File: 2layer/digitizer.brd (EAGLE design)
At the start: 88.9 x 88.9 mm, 40 parts, among them X1 SMA-142-0711-881/886

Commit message: started layout2
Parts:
- removed JP2: (no value), pinhead:1X10
- added X2: SMA-142-0711-881/886, con-coax:J502-ND-142-0711-881/886
- JP1: device pinhead:1X10 -> pinhead:2X20
- moved U$5 93.7 mm to (46.2, 44.0)
- moved JP1 69.7 mm to (-6.35, -88.6)
- moved C8 6.10 mm to (56.6, 35.3), turned to 270 degrees
- moved C7 4.75 mm to (58.2, 35.3), turned to 270 degrees
- moved C5 3.64 mm to (57.4, 37.3), turned to 0 degrees
- moved C6 3.45 mm to (57.4, 38.6), turned to 0 degrees
- moved X1 0.25 mm to (52.6, 88.4)
- moved C2 0.25 mm to (59.9, 37.6)
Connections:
- removed net SDC_OEN: JP2.4
- net ADC_SLP: no longer JP2.3
- net OVFL: no longer JP2.2
- net SAMP0: no longer JP1.1
- net SAMP1: no longer JP1.2
- net SAMP2: no longer JP1.3
- net SAMP3: no longer JP1.4
- net SAMP4: no longer JP1.5
- net SAMP5: no longer JP1.6
- net SAMP6: no longer JP1.7
- net SAMP7: no longer JP1.8
- net SAMP8: no longer JP1.9
- net SAMP9: no longer JP1.10
- net SAMPCLK: no longer JP2.1
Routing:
- net GND: track 5.53 -> 0.00 mm, vias 0 -> 8
- net AVDD: track 1.92 -> 0.00 mm

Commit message: starting final layout
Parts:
- added C15: (no value), rcl:C0402
- added C16, C17: 18p, resistor:C0402
- added C18, C19, C21: 0.1u, resistor:C0402
- added C20: 1u, resistor:C0402
- added C22: 4.7u, resistor:C0402
- added IC1: FT601QQFN76, lt_ftdi_and_more:QFN76
- added JP2: (no value), pinhead:2X20
- added JP3: (no value), pinhead:1X04
- added R10, R12, R13, R16, R17: (no value), resistor:R0402
- added R11: (no value), resistor:V234/12
- added R14, R15: 0, resistor:R0805
- added S1, S2: MOMENTARY-SWITCH-SPST-SMD-6.0X3.5MM, SparkFun-Switches:TACTILE_SWITCH_SMD_6.0X3.5MM
- added U$6: USB3.0, components:USB-MICROB-3.0
- added U$7: CX3225SB_UKY1C-H1-16357-0045, components:UKY1C-H1-16357-0045
- Z10, Z3, Z4, Z5: device components:R0805 -> components:R0402
- moved X2 147.9 mm to (0.51, 20.3)
- moved JP1 126.7 mm to (48.3, 25.7), turned to 90 degrees
- moved R6 97.8 mm to (17.5, 8.89), turned to 90 degrees
- moved X1 97.2 mm to (0.51, 6.35), turned to 0 degrees
- moved R7 96.7 mm to (17.5, 2.79), turned to 90 degrees
- moved Z11 91.3 mm to (17.5, 5.84), turned to 270 degrees
- moved R5 91.1 mm to (7.11, 2.29)
- moved Z6 88.2 mm to (7.11, 6.60), turned to 90 degrees
- moved Z10 85.8 mm to (18.8, 3.81), turned to 90 degrees
- moved Z8 84.1 mm to (9.37, 2.27), turned to 270 degrees
- moved C14 83.9 mm to (21.6, 9.91), turned to 270 degrees
- moved Z5 83.5 mm to (18.8, 6.86), turned to 270 degrees
- moved Z7 82.8 mm to (9.40, 6.60), turned to 90 degrees
- moved C13 82.4 mm to (24.1, 9.91), turned to 270 degrees
- moved Z9 76.7 mm to (8.38, 10.4), turned to 0 degrees
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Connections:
- removed net N$27: R6.1
- removed net N$28: R7.1
- new net BE0: IC1.4
- new net BE1: IC1.5
- new net BE2: IC1.6
- new net BE3: IC1.7
- new net D+: IC1.23, U$6.P$3
- new net D-: IC1.25, U$6.P$2
- new net FCLK: IC1.58
- new net GPIO0: IC1.17
- new net GPIO1: IC1.18
- new net N$11: C16.2, IC1.21, U$7.P$1
- new net N$12: C17.2, IC1.22, U$7.P$3
- new net N$13: IC1.27, R10.2, R11.2
- new net N$14: C18.2, U$6.P$10
- new net N$15: C19.2, U$6.P$9
- new net N$16: R14.1, X2.1
- new net OEN: IC1.13
- new net OTG_ID: U$6.P$4
- new net RDN: IC1.12
- new net RFIN2: JP3.2, R7.1
- new net RSTN: IC1.15, R12.2, R17.1, S2.2
- new net RXFN: IC1.9
- new net SFT_RSTN: R17.2
- new net SFT_WKPN: R16.2
- new net SIWUN: IC1.10
- new net SSRX+: IC1.35, U$6.P$7
- new net SSRX-: IC1.34, U$6.P$6
- new net SSTX+: C18.1, IC1.32
- new net SSTX-: C19.1, IC1.31
- new net TXEN: IC1.8
- new net UDAT0: IC1.40
- new net UDAT1: IC1.41
- new net UDAT10: IC1.52
- new net UDAT11: IC1.53
- new net UDAT12: IC1.54
- new net UDAT13: IC1.55
- new net UDAT14: IC1.56
- new net UDAT15: IC1.57
- new net UDAT16: IC1.60
- new net UDAT17: IC1.61
- new net UDAT18: IC1.62
- new net UDAT19: IC1.63
- new net UDAT2: IC1.42
- new net UDAT20: IC1.64
- new net UDAT21: IC1.65
- new net UDAT22: IC1.66
- new net UDAT23: IC1.67
- new net UDAT24: IC1.69
- new net UDAT25: IC1.70
- new net UDAT26: IC1.71
- new net UDAT27: IC1.72
- new net UDAT28: IC1.73
- new net UDAT29: IC1.74
- new net UDAT3: IC1.43
- new net UDAT30: IC1.75
- new net UDAT31: IC1.76
- new net UDAT4: IC1.44
- new net UDAT5: IC1.45
- new net UDAT6: IC1.46
- new net UDAT7: IC1.47
- new net UDAT8: IC1.50
- new net UDAT9: IC1.51
- new net V1REF: C15.2, C22.1, IC1.2, IC1.3, IC1.30, IC1.33, IC1.39, IC1.48
- new net VBUS: IC1.37, U$6.P$1
- new net WKPN: IC1.16, R13.2, R16.1, S1.2
- new net WRN: IC1.11
- net AVDD: now also JP3.4, R12.1, R13.1
- net DVDD: now also C20.1, C21.1, IC1.14, IC1.20, IC1.24, IC1.28, IC1.38, IC1.49, IC1.59, IC1.68
- net GND: now also C15.1, C16.1, C17.1, C20.2, C21.2, C22.2, IC1.1, IC1.26, IC1.29, IC1.36, IC1.77, JP3.1, R10.1, R11.1, R15.1, S1.1, S2.1, U$6.P$11, U$6.P$12, U$6.P$5, U$6.P$8, U$7.P$2, U$7.P$4, X2.G@1, X2.G@2, X2.G@3, X2.G@4
- net LO+: now also R14.2
- net LO-: now also R15.2
- net MIX+: now also U$5.6
- net MIX-: now also U$5.5
- net RFIN: now also JP3.3, R6.1
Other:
- board size 88.9 x 88.9 mm -> 88.1 x 52.3 mm

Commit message: okawndpam
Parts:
- removed JP3: (no value), pinhead:1X04
- removed R14, R15: 0, resistor:R0805
- removed R5: 25, resistor:R0805
- removed Z6: 12p, resistor:C0805
- removed Z7, Z9: 0, components:R0805
- removed Z8: 0, resistor:C0805
- moved C16 74.5 mm to (15.2, 39.9), turned to 270 degrees
- moved U$7 70.7 mm to (18.3, 39.9), turned to 0 degrees
- moved C18 67.6 mm to (16.3, 43.9), turned to 90 degrees
- moved R10 67.3 mm to (11.4, 43.7), turned to 270 degrees
- moved R11 67.3 mm to (11.4, 43.7), turned to 270 degrees
- moved JP2 67.1 mm to (121.5, 26.7)
- moved C17 66.9 mm to (21.3, 39.9), turned to 90 degrees
- moved JP1 64.3 mm to (112.5, 26.9)
- moved C19 63.8 mm to (17.8, 43.9), turned to 90 degrees
- moved U$6 61.3 mm to (24.2, 47.1), turned to 180 degrees
- moved S2 59.0 mm to (2.79, 46.5), turned to 270 degrees
- moved R17 57.0 mm to (3.81, 40.1), turned to 270 degrees
- moved S1 56.9 mm to (7.11, 46.5), turned to 270 degrees
- moved R16 56.5 mm to (5.84, 39.9), turned to 270 degrees
- moved X1 55.5 mm to (55.6, 0.25), turned to 90 degrees
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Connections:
- removed net N$16: R14.1, X2.1
- removed net RFILT: Z7.2, Z8.1, Z9.1
- removed net RFIN: JP3.3, R6.1, Z9.2
- removed net RFIN2: JP3.2, R7.1
- net AVDD: no longer JP3.4
- net GND: now also JP1.11, JP1.12, JP1.21, JP1.22, JP1.31, JP2.21, JP2.22, JP2.31, JP2.32; no longer JP3.1, R15.1, X1.G@1, X1.G@2, X1.G@3, X1.G@4, X2.G@1, X2.G@2, X2.G@3, X2.G@4, Z6.2, Z8.2
- net LO+: now also X2.1; no longer R14.2
- net LO-: now also X2.G@1, X2.G@2, X2.G@3, X2.G@4; no longer R15.2
- net N$1: now also R7.1, X1.G@1, X1.G@2, X1.G@3, X1.G@4; no longer R5.2, Z6.1, Z7.1
- net N$10: now also R6.1; no longer R5.1
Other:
- board size 88.1 x 52.3 mm -> 75.7 x 51.3 mm

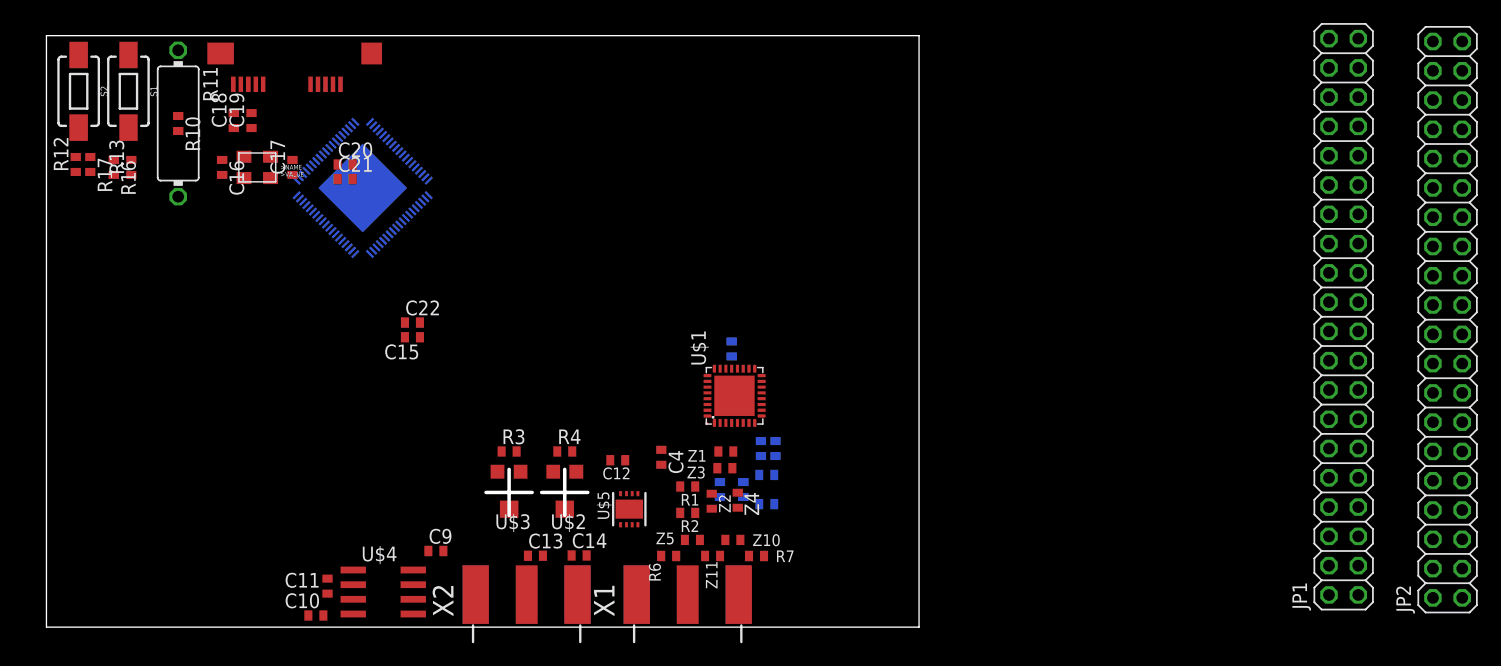
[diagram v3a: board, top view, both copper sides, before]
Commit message: moved guts to center to make more of a sheild-like adaptor to mate with MACH
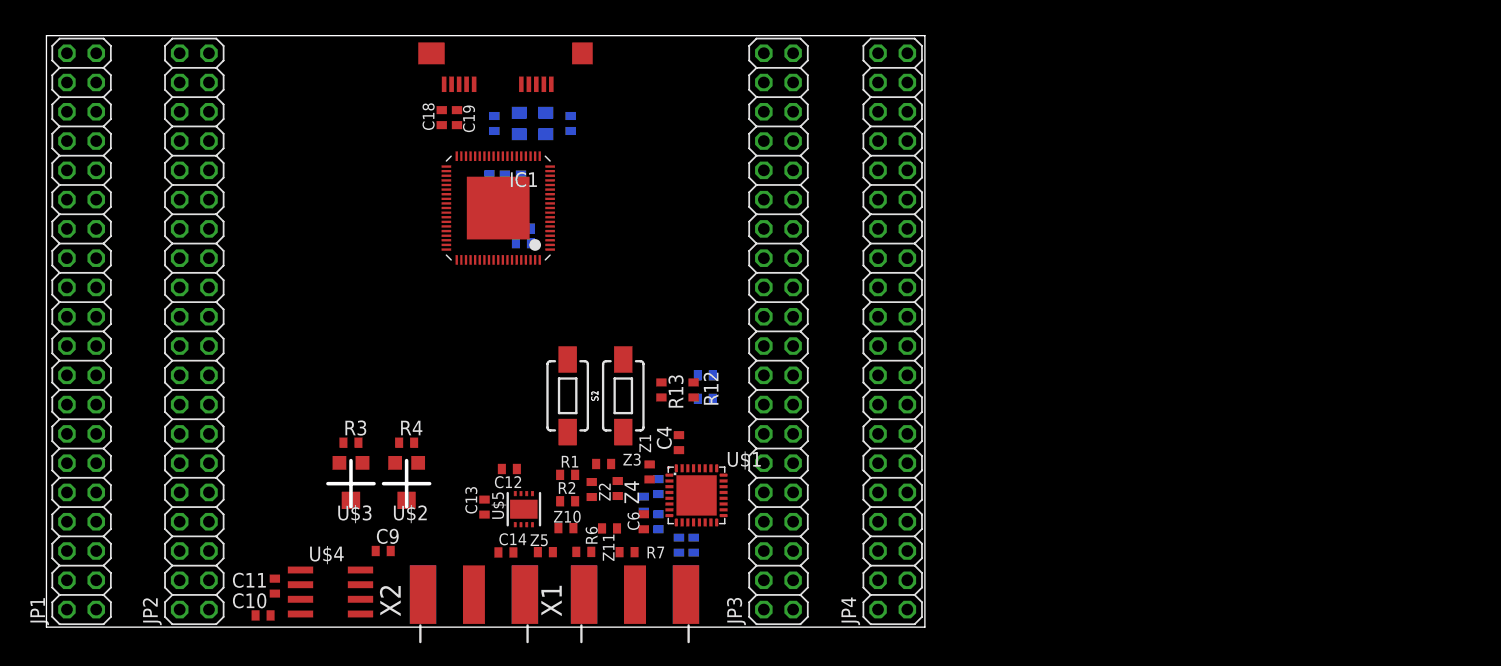
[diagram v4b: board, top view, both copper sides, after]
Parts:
- removed R11: (no value), resistor:V234/12
- added JP3, JP4: (no value), pinhead:2X20
- R10: value (none) -> 10k <=0.1%
- moved JP1 109.5 mm to (3.05, 25.7)
- moved JP2 108.7 mm to (12.8, 25.7)
- moved R17 57.1 mm to (57.1, 19.8), flipped to the bottom, turned to 180 degrees
- moved R12 57.1 mm to (56.1, 20.6), turned to 270 degrees
- moved R16 54.4 mm to (57.1, 21.8), flipped to the bottom, turned to 180 degrees
- moved S1 50.4 mm to (50.0, 20.1), turned to 90 degrees
- moved S2 50.0 mm to (45.2, 20.1), turned to 90 degrees
- moved R13 49.9 mm to (53.3, 20.6)
- moved C16 30.5 mm to (45.5, 43.7), flipped to the bottom
- moved R10 30.2 mm to (41.2, 38.6), flipped to the bottom, turned to 90 degrees
- moved U$7 24.2 mm to (42.2, 43.7), flipped to the bottom
- moved U$6 18.3 mm to (42.5, 47.1)
- moved C18 18.0 mm to (34.3, 44.2)
- moved C17 17.9 mm to (38.9, 43.7), flipped to the bottom
- moved C19 17.8 mm to (35.6, 44.2)
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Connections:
- net GND: no longer R11.1
- net N$13: no longer R11.2
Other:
- board size 75.7 x 51.3 mm -> 76.2 x 51.3 mm

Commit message: started meandering fifo bus
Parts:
- removed S1, S2: MOMENTARY-SWITCH-SPST-SMD-6.0X3.5MM, SparkFun-Switches:TACTILE_SWITCH_SMD_6.0X3.5MM
- added RESET, USB_WAKE: MOMENTARY-SWITCH-SPST-SMD-6.0X3.5MM, SparkFun-Switches:TACTILE_SWITCH_SMD_6.0X3.5MM
- moved R17 27.7 mm to (56.9, 47.5)
- moved R12 26.9 mm to (49.0, 46.5)
- moved R13 25.9 mm to (54.6, 46.5), turned to 270 degrees
- moved R16 23.9 mm to (56.9, 45.7)
- moved C16 10.3 mm to (41.9, 34.0), turned to 180 degrees
- moved C15 10.1 mm to (32.3, 28.9), turned to 225 degrees
- moved C22 9.48 mm to (33.2, 29.8), turned to 45 degrees
- moved U$7 8.64 mm to (41.9, 35.1), flipped to the top, turned to 90 degrees
- moved C17 8.21 mm to (41.9, 36.1), turned to 0 degrees
- moved R10 7.83 mm to (35.9, 32.8), turned to 135 degrees
- moved IC1 7.32 mm to (32.9, 32.6), turned to 135 degrees
- moved C20 6.83 mm to (34.9, 33.8), turned to 315 degrees
- moved C21 5.90 mm to (34.0, 34.8), turned to 315 degrees
- moved R7 3.05 mm to (53.4, 6.50)
- moved R6 2.29 mm to (48.9, 6.53)
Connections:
- new net GND1: JP4.32
- new net GND2: JP4.22
- new net GND3: JP4.12
- new net GND4: JP4.11
- new net GND5: JP4.21
- new net GND6: JP4.31
- net BE0: now also JP4.24
- net BE1: now also JP4.23
- net BE2: now also JP4.26
- net BE3: now also JP4.25
- net FCLK: now also JP1.25
- net GND: now also JP2.11, JP2.12, RESET.1, USB_WAKE.1; no longer S1.1, S2.1
- net GPIO0: now also JP3.28
- net GPIO1: now also JP3.27
- net OEN: now also JP3.26
- net RDN: now also JP3.25
- net RSTN: now also RESET.2; no longer S2.2
- net RXFN: now also JP3.21
- net SIWUN: now also JP3.23
- net TXEN: now also JP3.22
- net UDAT0: now also JP2.39
- net UDAT1: now also JP2.40
- net UDAT10: now also JP1.29
- net UDAT11: now also JP1.30
- net UDAT12: now also JP2.28
- net UDAT13: now also JP2.27
- net UDAT14: now also JP1.27
- net UDAT15: now also JP1.28
- net UDAT16: now also JP2.26
- net UDAT17: now also JP2.25
- net UDAT18: now also JP2.24
- net UDAT19: now also JP1.24, JP2.23
- net UDAT2: now also JP2.37
- net UDAT20: now also JP1.23
- net UDAT22: now also JP1.19
- net UDAT23: now also JP1.20
- net UDAT24: now also JP2.20
- net UDAT25: now also JP2.19
- net UDAT26: now also JP2.18
- net UDAT27: now also JP2.17
- net UDAT28: now also JP2.16
- net UDAT29: now also JP2.15
- net UDAT3: now also JP2.38
- net UDAT30: now also JP2.14
- net UDAT31: now also JP2.13
- net UDAT4: now also JP2.35
- net UDAT5: now also JP2.36
- net UDAT6: now also JP2.33
- net UDAT7: now also JP2.34
- net UDAT8: now also JP2.30
- net UDAT9: now also JP2.29
- net WKPN: now also USB_WAKE.2; no longer S1.2
- net WRN: now also JP3.24
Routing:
- net UDAT15: track 0.00 -> 26.4 mm
- net UDAT14: track 0.00 -> 25.8 mm
- net UDAT12: track 0.00 -> 25.7 mm
- net UDAT13: track 0.00 -> 24.9 mm
- net FCLK: track 0.00 -> 23.9 mm, vias 0 -> 1
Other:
- outline, holes or cut-outs redrawn

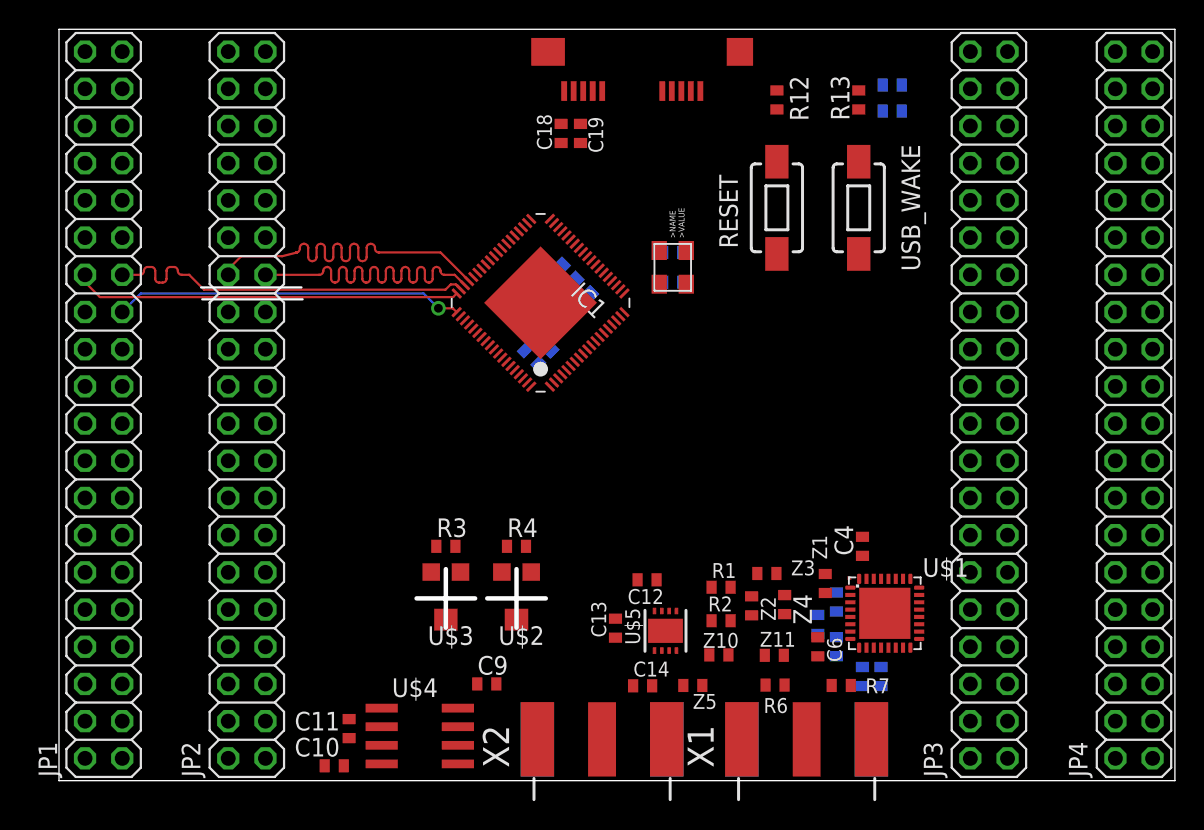
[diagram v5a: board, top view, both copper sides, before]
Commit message: fixed header positions to match mach
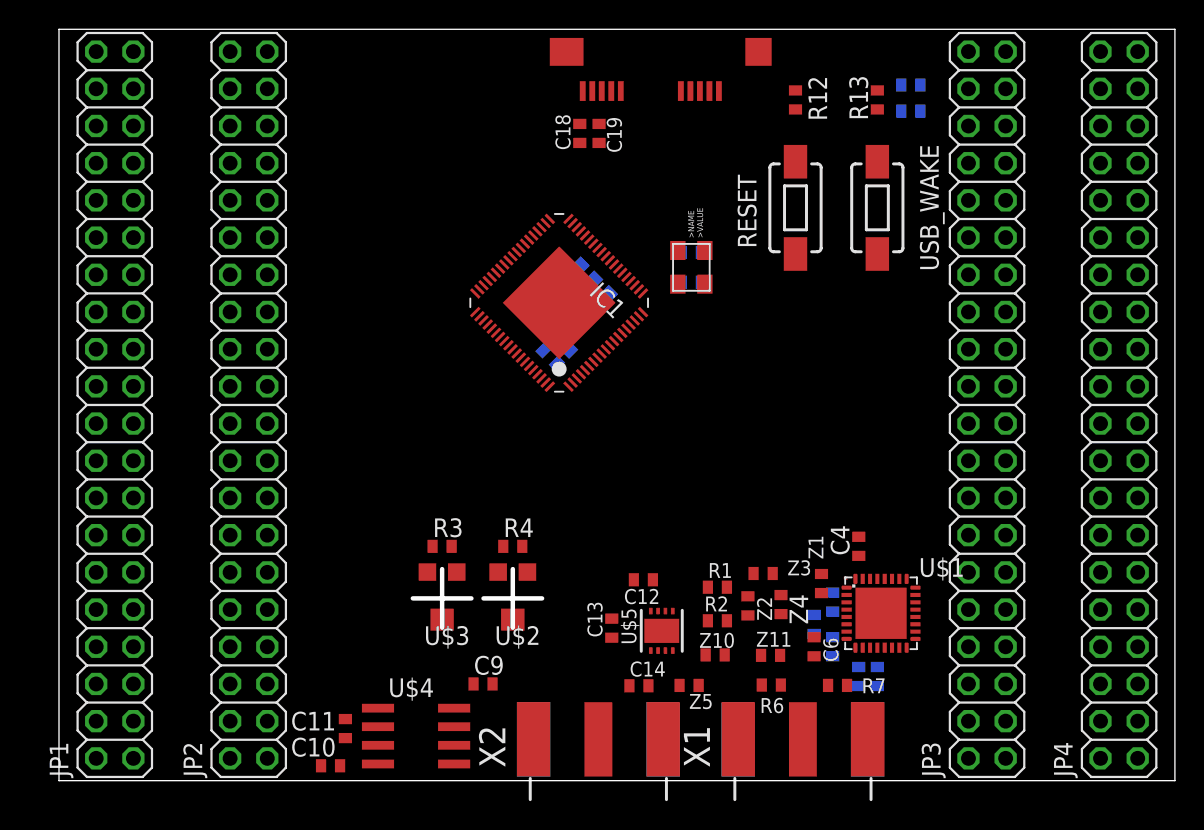
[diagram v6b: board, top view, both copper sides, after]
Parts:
- moved C15 1.27 mm to (33.5, 28.9)
- moved C16 1.27 mm to (43.2, 34.0)
- moved C17 1.27 mm to (43.2, 36.1)
- moved C18 1.27 mm to (35.6, 44.2)
- moved C19 1.27 mm to (36.9, 44.2)
- moved C21 1.27 mm to (35.2, 34.8)
- moved IC1 1.27 mm to (34.2, 32.6)
- moved R10 1.27 mm to (37.2, 32.8)
- moved R12 1.27 mm to (50.3, 46.5)
- moved R13 1.27 mm to (55.9, 46.5)
- moved RESET 1.27 mm to (50.3, 39.1)
- moved U$6 1.27 mm to (43.8, 47.1)
- moved U$7 1.27 mm to (43.2, 35.1)
- moved USB_WAKE 1.27 mm to (55.9, 39.1)
- moved C20 1.27 mm to (36.2, 33.8)
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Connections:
- removed net GND1: JP4.32
- removed net GND2: JP4.22
- removed net GND3: JP4.12
- removed net GND4: JP4.11
- removed net GND5: JP4.21
- removed net GND6: JP4.31
- net GND: now also JP3.21, JP3.22, JP4.11, JP4.12, JP4.21, JP4.22, JP4.31, JP4.32
- net RXFN: no longer JP3.21
- net TXEN: no longer JP3.22
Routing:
- net UDAT15: track 26.4 -> 0.00 mm
- net UDAT14: track 25.8 -> 0.00 mm
- net UDAT12: track 25.7 -> 0.00 mm
- net UDAT13: track 24.9 -> 0.00 mm
- net FCLK: track 23.9 -> 0.00 mm, vias 1 -> 0
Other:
- outline, holes or cut-outs redrawn

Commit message: almost done allocating wires
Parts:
- moved Z11 2.49 mm to (46.6, 7.09), turned to 90 degrees
- moved R17 2.30 mm to (58.4, 49.8)
- moved Z3 1.69 mm to (49.8, 13.9)
- moved R16 1.55 mm to (58.4, 47.2)
- moved Z10 1.27 mm to (43.8, 7.82)
- moved R7 1.27 mm to (51.9, 6.50)
- moved R2 1.14 mm to (45.5, 11.9)
- moved Z2 1.14 mm to (47.5, 13.0)
- moved R1 0.92 mm to (45.5, 14.0)
- moved Z1 0.57 mm to (51.8, 13.0)
- moved U$5 0.51 mm to (41.2, 10.7)
- moved Z4 0.47 mm to (49.8, 12.0), turned to 0 degrees
- moved C6 0.36 mm to (51.8, 9.40), turned to 270 degrees
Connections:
- net ADC_OEN: now also JP4.4
- net ADC_SLP: now also JP4.3
- net BE0: now also JP3.18; no longer JP4.24
- net BE1: now also JP3.17; no longer JP4.23
- net BE2: now also JP3.20; no longer JP4.26
- net BE3: now also JP3.19; no longer JP4.25
- net GND: now also JP3.11, JP3.12, JP3.31, JP3.32, JP3.39
- net GPIO0: now also JP3.29; no longer JP3.28
- net GPIO1: now also JP3.30; no longer JP3.27
- net OEN: now also JP3.28; no longer JP3.26
- net OVFL: now also JP3.16
- net RDN: now also JP3.27; no longer JP3.25
- net RXFN: now also JP3.24
- net SAMP0: now also JP3.3
- net SAMP1: now also JP3.6
- net SAMP2: now also JP3.5
- net SAMP3: now also JP3.8
- net SAMP4: now also JP3.7
- net SAMP5: now also JP3.10
- net SAMP6: now also JP3.9
- net SAMP7: now also JP3.13
- net SAMP8: now also JP3.14
- net SAMP9: now also JP3.15
- net SAMPCLK: now also JP3.4
- net SFT_RSTN: now also JP3.40
- net SFT_WKPN: now also JP3.38
- net SIWUN: now also JP3.25; no longer JP3.23
- net TXEN: now also JP3.23
- net WRN: now also JP3.26; no longer JP3.24
